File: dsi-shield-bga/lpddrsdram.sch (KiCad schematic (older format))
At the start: 2 parts, among them U2 MT48LC16M16A2F4, U3 MT48LC16M16A2F4

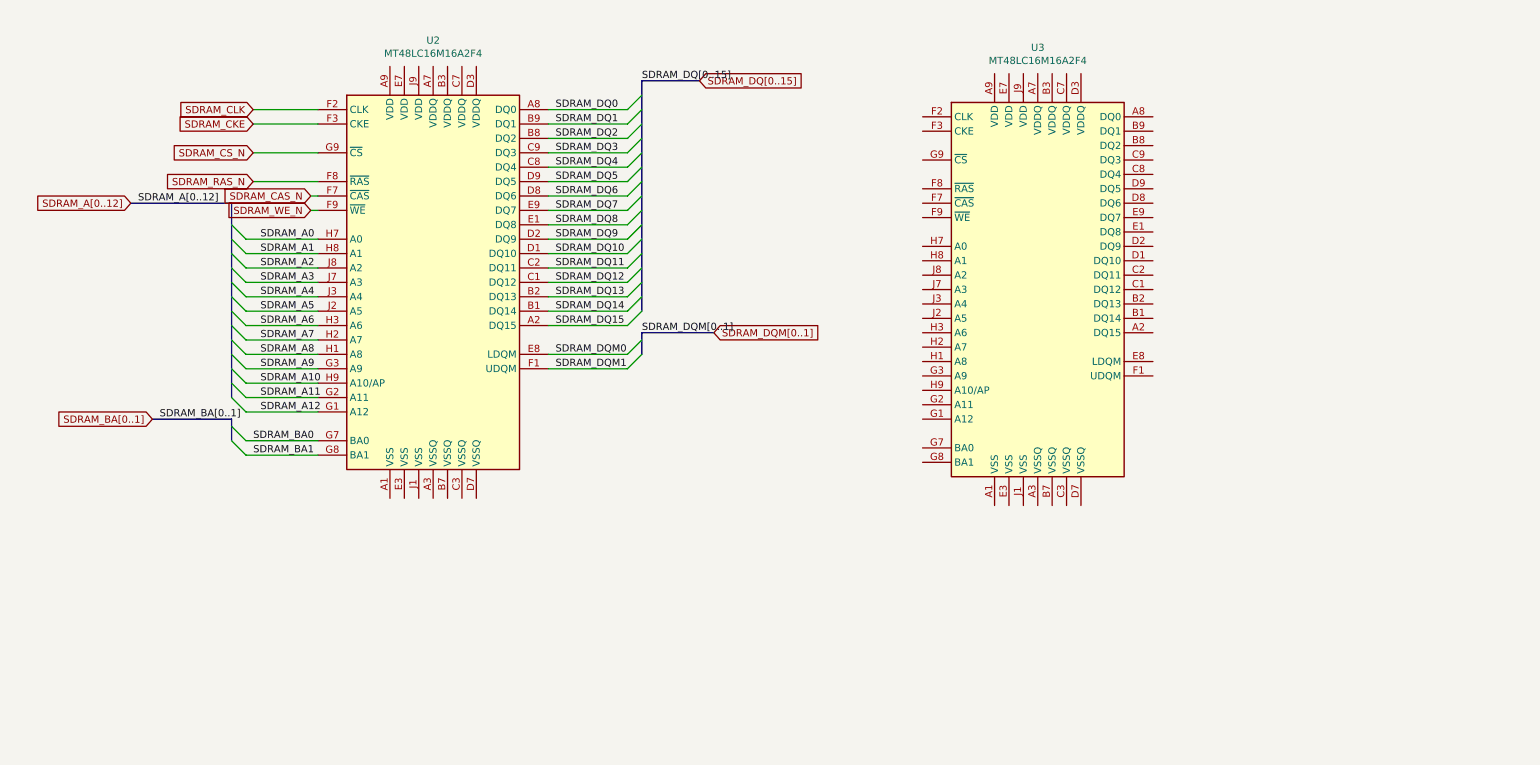
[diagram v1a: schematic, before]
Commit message: ddr sdram
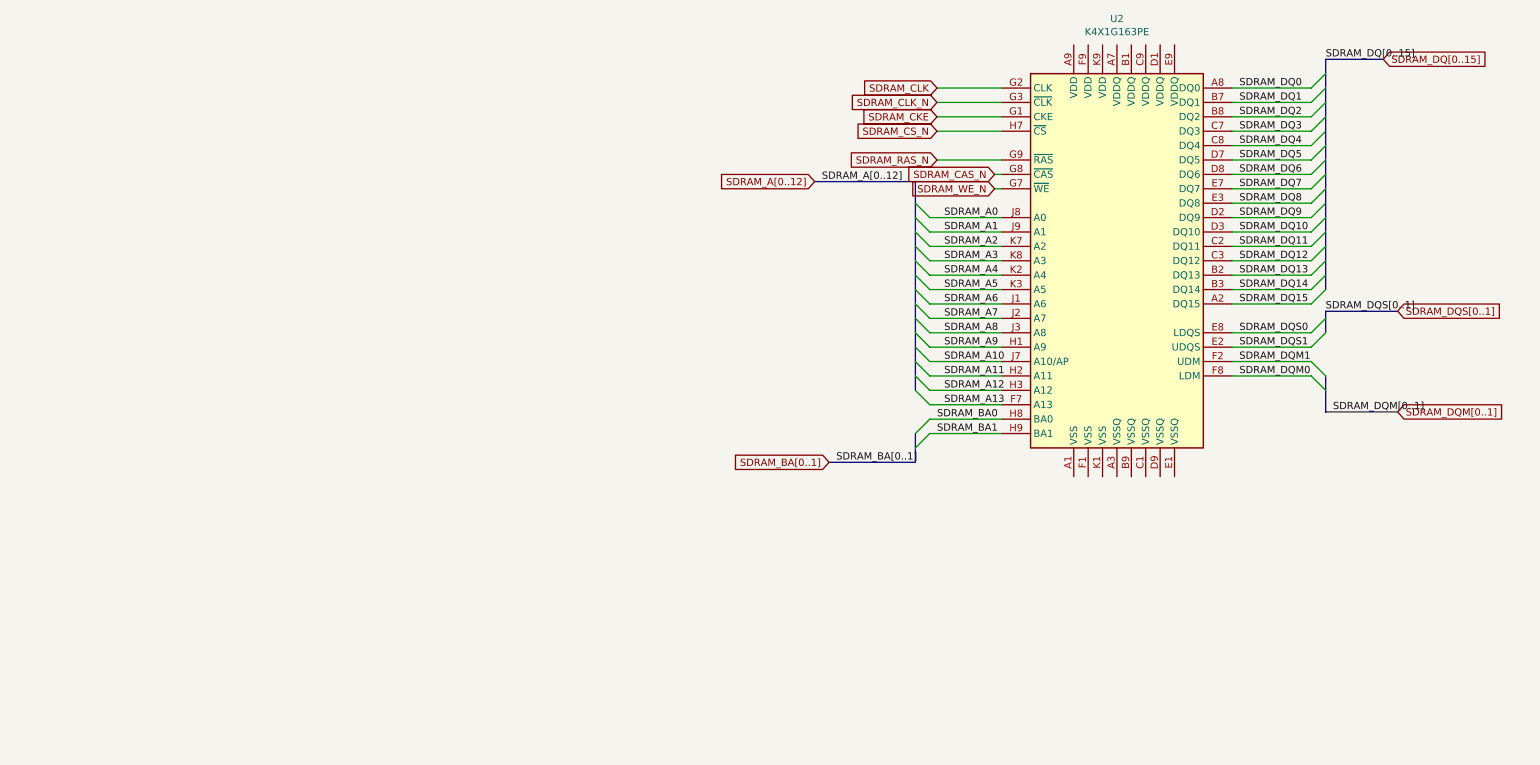
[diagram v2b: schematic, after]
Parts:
- removed U2, U3: MT48LC16M16A2F4, Gekkio_Package_BGA:Micron_VFBGA-54_8x14mm_Layout9x9_P0.8mm, symbol Gekkio_Package_BGA:MT48LC16M16A2F4
- added U2: K4X1G163PE, mybays:FBGA60-6X10, symbol mybays:K4X1G163PE
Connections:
- net SDRAM_A0: now also U2.J8 (A0)
- net SDRAM_A1: now also U2.J9 (A1)
- net SDRAM_A10: now also U2.J7 (A10/AP)
- net SDRAM_A11: now also U2.H2 (A11)
- net SDRAM_A12: now also U2.H3 (A12)
- net SDRAM_A2: now also U2.K7 (A2)
- net SDRAM_A3: now also U2.K8 (A3)
- net SDRAM_A4: now also U2.K2 (A4)
- net SDRAM_A5: now also U2.K3 (A5)
- net SDRAM_A6: now also U2.J1 (A6)
- net SDRAM_A7: now also U2.J2 (A7)
- net SDRAM_A8: now also U2.J3 (A8)
- net SDRAM_A9: now also U2.H1 (A9)
- net SDRAM_BA0: now also U2.H8 (BA0)
- net SDRAM_BA1: now also U2.H9 (BA1)
- net SDRAM_CAS_N: now also U2.G8 (~CAS)
- net SDRAM_CKE: now also U2.G1 (CKE)
- net SDRAM_CLK: now also U2.G2 (CLK)
- net SDRAM_CS_N: now also U2.H7 (~CS)
- net SDRAM_DQ0: now also U2.A8 (DQ0)
- net SDRAM_DQ1: now also U2.B7 (DQ1)
- net SDRAM_DQ10: now also U2.D3 (DQ10)
- net SDRAM_DQ11: now also U2.C2 (DQ11)
- net SDRAM_DQ12: now also U2.C3 (DQ12)
- net SDRAM_DQ13: now also U2.B2 (DQ13)
- net SDRAM_DQ14: now also U2.B3 (DQ14)
- net SDRAM_DQ15: now also U2.A2 (DQ15)
- net SDRAM_DQ2: now also U2.B8 (DQ2)
- net SDRAM_DQ3: now also U2.C7 (DQ3)
- net SDRAM_DQ4: now also U2.C8 (DQ4)
- net SDRAM_DQ5: now also U2.D7 (DQ5)
- net SDRAM_DQ6: now also U2.D8 (DQ6)
- net SDRAM_DQ7: now also U2.E7 (DQ7)
- net SDRAM_DQ8: now also U2.E3 (DQ8)
- net SDRAM_DQ9: now also U2.D2 (DQ9)
- net SDRAM_DQM0: now also U2.F8 (LDM)
- net SDRAM_DQM1: now also U2.F2 (UDM)
- net SDRAM_RAS_N: now also U2.G9 (~RAS)
- net SDRAM_WE_N: now also U2.G7 (~WE)
- new net SDRAM_A13: U2.F7 (A13)
- new net SDRAM_CLK_N: U2.G3 (~CLK)
- new net SDRAM_DQS0: U2.E8 (LDQS)
- new net SDRAM_DQS1: U2.E2 (UDQS)

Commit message: 20200808
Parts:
- added C20: 1u, Capacitor_SMD:C_0402_1005Metric, symbol dsi_shield:Cap
- added C21, C22, C23, C24, C25, C26: 100n, Capacitor_SMD:C_0402_1005Metric, symbol dsi_shield:Cap
- added C27, C28, C29: 10n, Capacitor_SMD:C_0402_1005Metric, symbol dsi_shield:Cap
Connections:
- net GND: now reaches U2.A1 (VSS)
- net GND: now also U2.A3 (VSSQ), U2.B9 (VSSQ), U2.C1 (VSSQ), U2.D9 (VSSQ), U2.E1 (VSSQ), U2.F1 (VSS), U2.K1 (VSS), C20.2, C21.2, C22.2, C23.2, C24.2, C25.2, C26.2, C27.2, C28.2, C29.2
- net V_DDR: now reaches U2.A7 (VDDQ)
- net V_DDR: now also U2.A9 (VDD), U2.B1 (VDDQ), U2.C9 (VDDQ), U2.D1 (VDDQ), U2.E9 (VDDQ), U2.F9 (VDD), U2.K9 (VDD), C20.1, C21.1, C22.1, C23.1, C24.1, C25.1, C26.1, C27.1, C28.1, C29.1
- net SDRAM_CLK renamed SDRAM_CLK_P
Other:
- moved on the sheet: U2
